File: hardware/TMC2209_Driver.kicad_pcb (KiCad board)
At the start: 2 copper layers, 36.7 x 39.4 mm, 30 parts, among them J1 PCIe_Stepper, J2 Conn_01x04_Male, U1 TMC2209-LA, U2 74LVC1G06, U3 24LC02

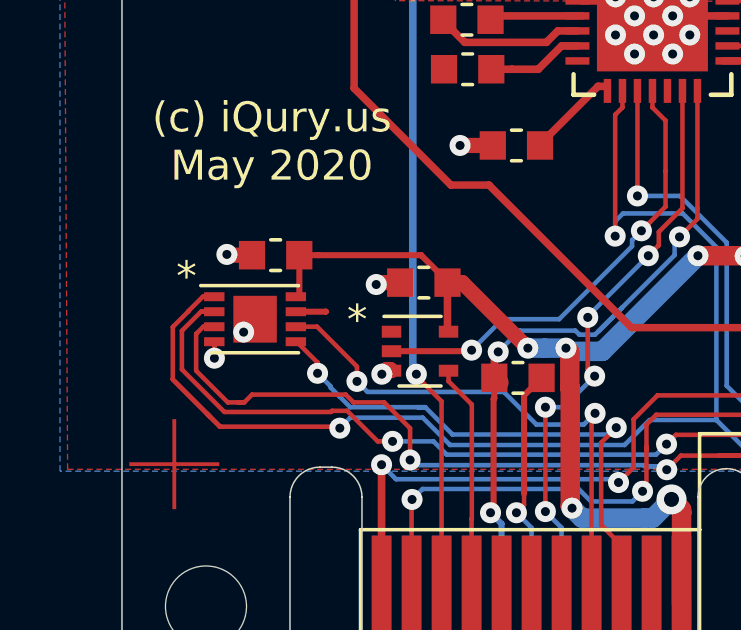
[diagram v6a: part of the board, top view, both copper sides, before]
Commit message: Updated DRC rules. Fix labels.
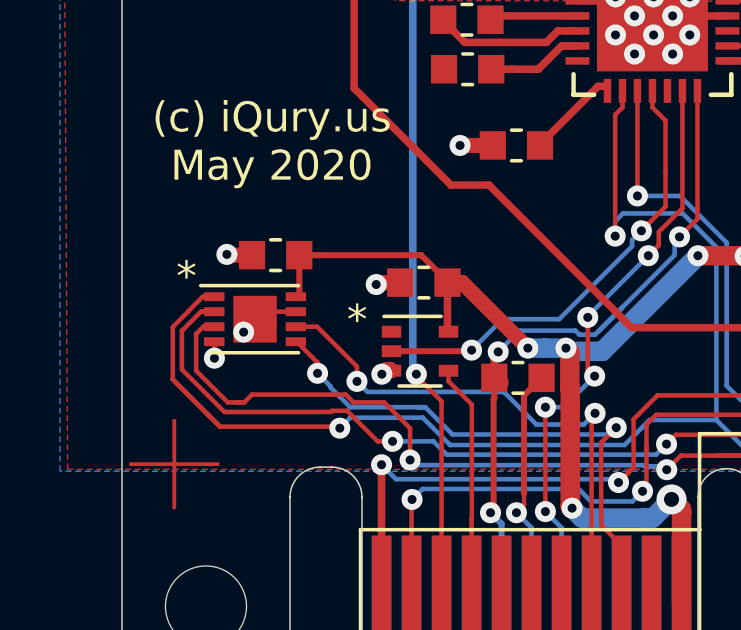
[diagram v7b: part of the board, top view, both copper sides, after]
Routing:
- net GND: track 51.2 -> 51.8 mm
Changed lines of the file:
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@@
     (pcbplotparams
       (layerselection 0x00010fc_ffffffff)
+      (disableapertmacros false)
       (usegerberextensions true)
       (usegerberattributes false)
@@
       (svgprecision 6)
       (excludeedgelayer true)
-      (linewidth 0.100000)
       (plotframeref false)
       (viasonmask false)
@@
   (segment (start 112.081143 102.043624) (end 112.081143 102.467888) (width 0.1524) (layer "F.Cu") (net 2))
   (segment (start 112.522 99.0346) (end 112.4966 99.0092) (width 0.508) (layer "F.Cu") (net 2))
-  (segment (start 114.9118 100.9182) (end 115.7946 100.9182) (width 0.2032) (layer "F.Cu") (net 2))
   (segment (start 140.846 86.36) (end 140.846 84.331) (width 1.5) (layer "F.Cu") (net 2))
   (segment (start 131.826 87.122) (end 133.35 87.122) (width 0.508) (layer "F.Cu") (net 2))
@@
   (segment (start 143.45 102.25) (end 143.45 102.05) (width 0.65) (layer "F.Cu") (net 2))
   (segment (start 133.3755 93.599) (end 134.493 93.599) (width 0.508) (layer "F.Cu") (net 2))
-  (segment (start 115.7946 100.9182) (end 115.7986 100.9142) (width 0.2032) (layer "F.Cu") (net 2))
+  (segment (start 114.7964 100.9182) (end 113.6864 100.9182) (width 0.1524) (layer "F.Cu") (net 2))
   (segment (start 143.45 102.45) (end 144.5 103.5) (width 0.65) (layer "F.Cu") (net 2))
   (segment (start 127.682501 92.573599) (end 127.9271 92.329) (width 0.254) (layer "F.Cu") (net 2))
@@
   (segment (start 127.682501 90.058999) (end 126.6825 91.059) (width 0.254) (layer "F.Cu") (net 2))
   (segment (start 129.1825 91.059) (end 126.6825 91.059) (width 0.254) (layer "F.Cu") (net 2))
+  (segment (start 113.6864 100.9182) (end 113.4364 101.1682) (width 0.1524) (layer "F.Cu") (net 2))
   (segment (start 124.3354 90.559001) (end 126.182501 90.559001) (width 0.254) (layer "F.Cu") (net 2))
   (segment (start 126.6825 90.3859) (end 126.7206 90.424) (width 0.254) (layer "F.Cu") (net 2))

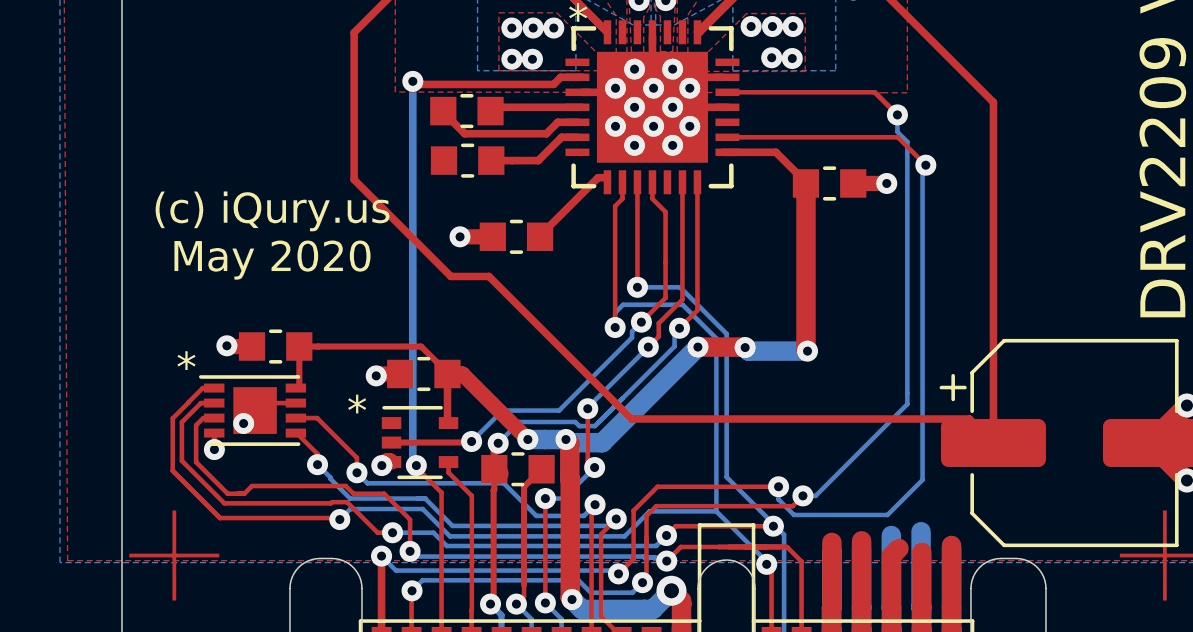
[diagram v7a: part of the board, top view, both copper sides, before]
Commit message: Added jumper for the TMC2209 driver clock selection.
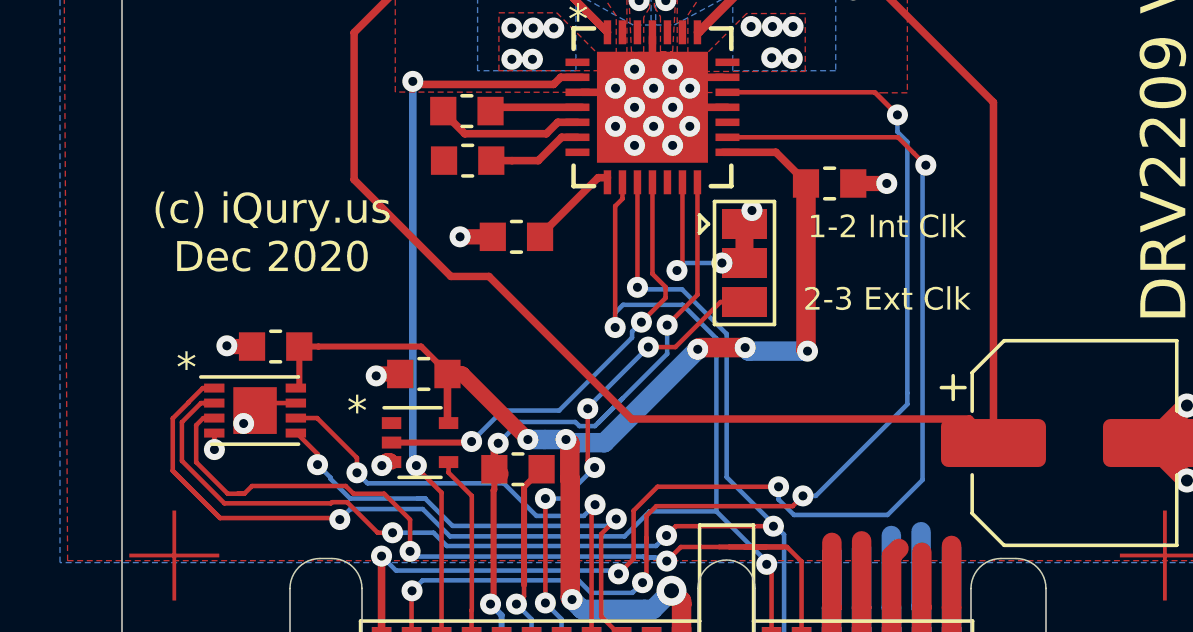
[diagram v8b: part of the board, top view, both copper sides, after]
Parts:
- added JP1: ClkIn, Jumper:SolderJumper-3_P1.3mm_Bridged12_Pad1.0x1.5mm, F.Cu at (129.8, 96.2)
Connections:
- U1 pad 13: /CLOCK -> Net-(JP1-Pad2)
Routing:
- net Net-(JP1-Pad2): track 0.00 -> 5.37 mm, vias 0 -> 2
- net /CLOCK: track 19.8 -> 17.6 mm
- net GND: track 51.8 -> 52.4 mm, vias 39 -> 40
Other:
- board text added: "(c) iQury.us Dec 2020"
- board text added: "1-2 Int Clk 2-3 Ext Clk"
- board text removed: "(c) iQury.us May 2020"
